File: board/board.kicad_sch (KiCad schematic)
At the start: 19 parts, among them J1 UART, J2 008_USB, J3 DebugEdge_02x05, J4 SPI_2x3, J5 ADC_2x3, J6 021_single_IO_UNIO, J7 SPI_2x3, J8 I2C_2x2, J9 UART_2x2

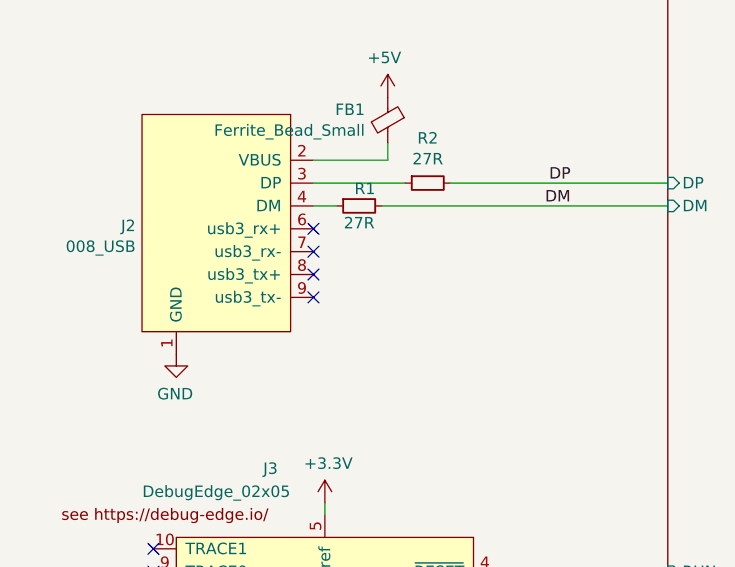
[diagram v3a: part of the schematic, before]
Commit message: upgraded to new kicad and switched to standard flash
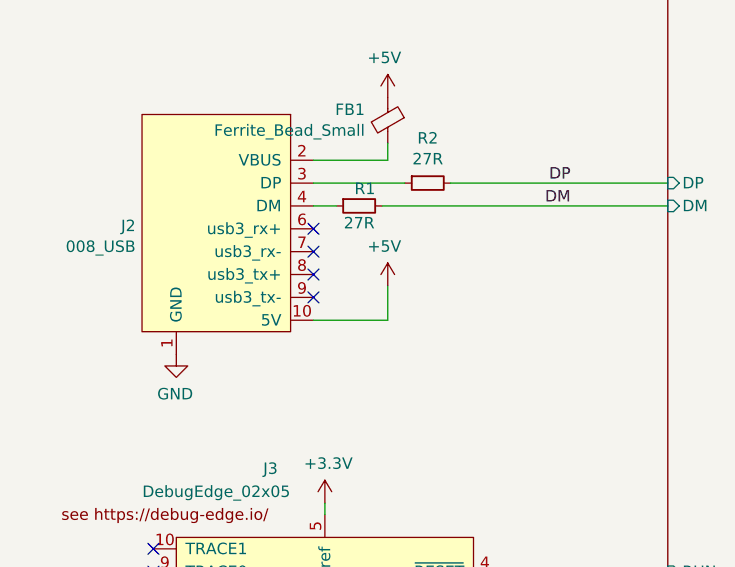
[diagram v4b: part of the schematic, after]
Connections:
- net +5V: now also J2.10 (5V)
- net +3V3 renamed +3.3V

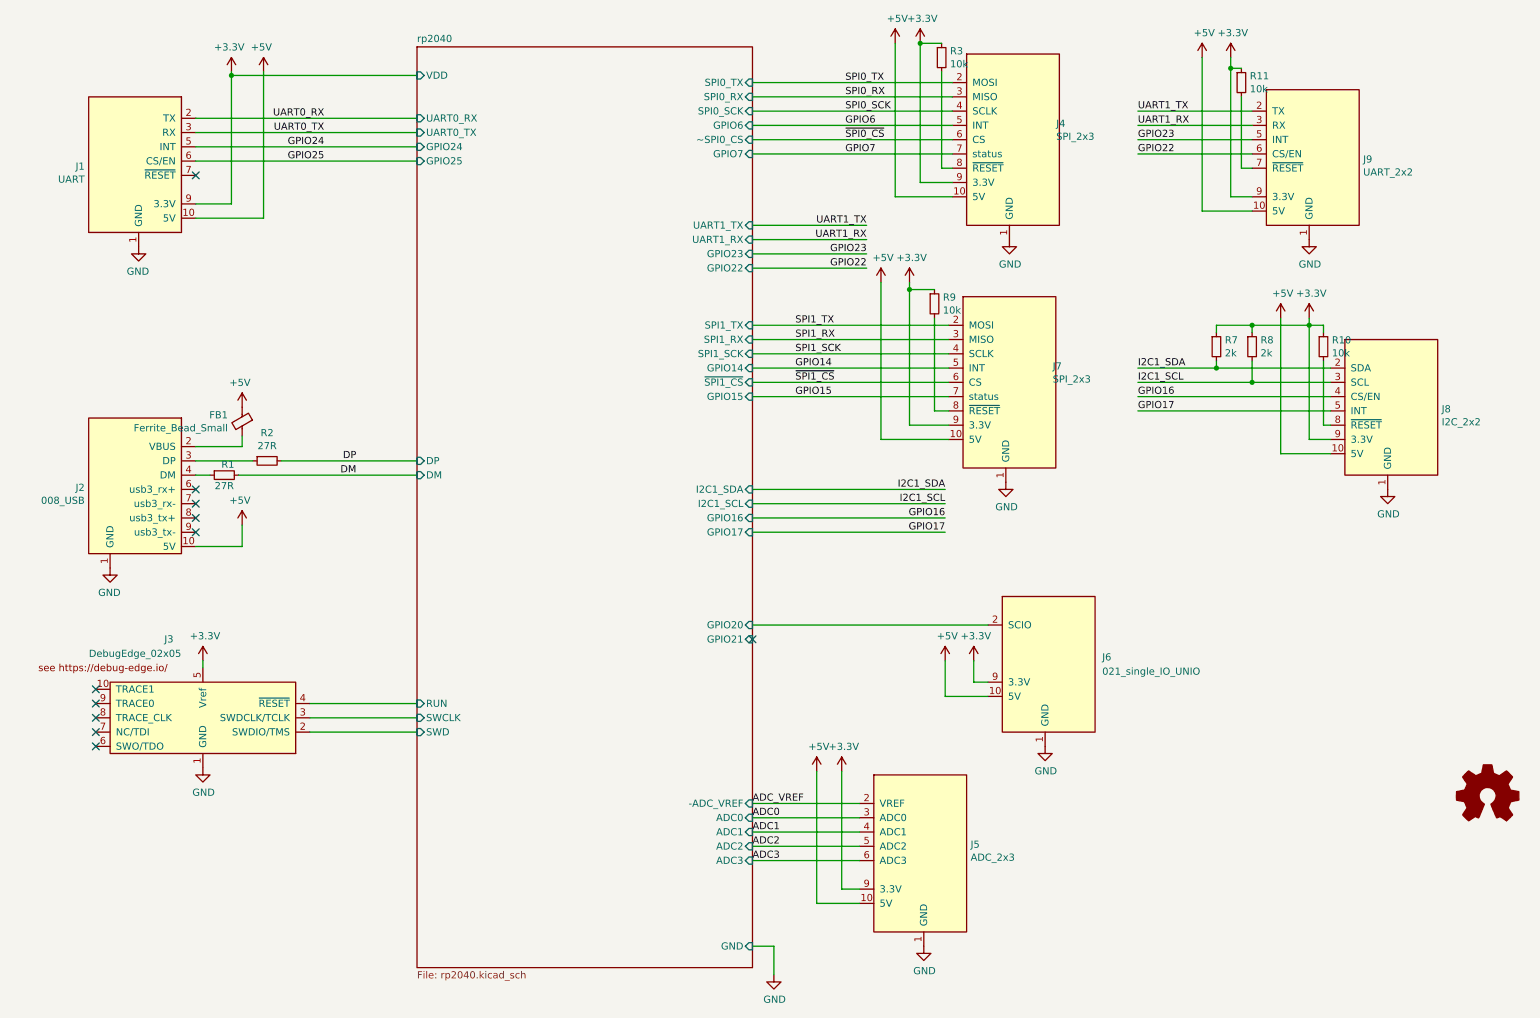
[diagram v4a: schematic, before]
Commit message: updated I2C to fixed pinning
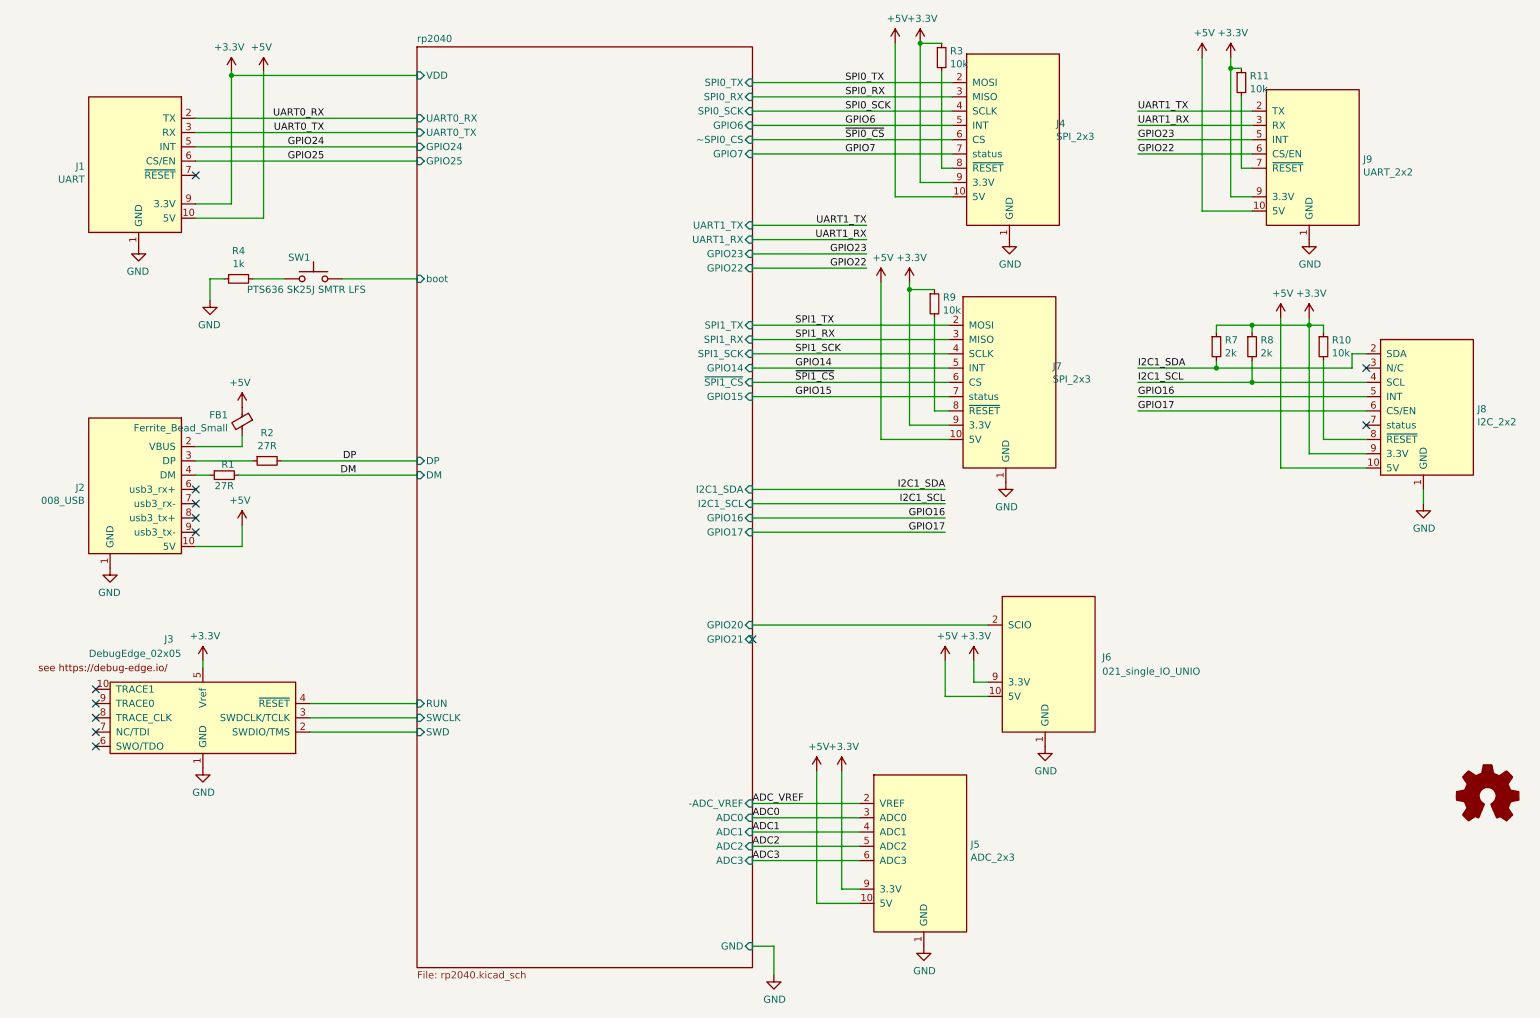
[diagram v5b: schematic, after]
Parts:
- added R4: 1k, Resistor_SMD:R_0603_1608Metric, symbol Device:R_Small
- added SW1: PTS636 SK25J SMTR LFS, Resistor_SMD:R_2512_6332Metric, symbol Switch:SW_Push
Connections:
- net GND: now also R4.1
- net GPIO16: now also J8.5 (INT); no longer J8.4 (CS/EN)
- net GPIO17: now also J8.6 (CS/EN); no longer J8.5 (INT)
- net I2C1_SCL: now also J8.4 (SCL); no longer J8.3 (SCL)
- new net: R4.2, SW1.1
- new net rp2040/boot: SW1.2
- no-connect marks 11 -> 13
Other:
- sheet rp2040 ports: added boot; removed none
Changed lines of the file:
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@@
   (no_connect (at 43.18 104.14))
   (no_connect (at 43.18 43.18))
+  (no_connect (at 251.46 77.47))
   (no_connect (at 142.24 125.73))
   (no_connect (at 25.4 142.24))
   (no_connect (at 43.18 99.06))
   (no_connect (at 43.18 106.68))
+  (no_connect (at 251.46 87.63))
   (no_connect (at 25.4 139.7))
   (no_connect (at 43.18 101.6))
@@
     (stroke (width 0) (type default))
   )
+  (wire (pts (xy 261.62 101.6) (xy 261.62 99.06))
+    (stroke (width 0) (type default))
+  )
   (wire (pts (xy 51.435 109.22) (xy 51.435 105.41))
     (stroke (width 0) (type default))
@@
     (stroke (width 0) (type default))
   )
+  (wire (pts (xy 45.72 61.595) (xy 48.26 61.595))
+    (stroke (width 0) (type default))
+  )
   (wire (pts (xy 142.24 123.19) (xy 184.15 123.19))
     (stroke (width 0) (type default))
@@
     (stroke (width 0) (type default))
   )
+  (wire (pts (xy 69.215 61.595) (xy 82.55 61.595))
+    (stroke (width 0) (type default))
+  )
   (wire (pts (xy 146.05 180.34) (xy 142.24 180.34))
     (stroke (width 0) (type default))
   )
-  (wire (pts (xy 241.3 90.17) (xy 245.11 90.17))
+  (wire (pts (xy 241.3 92.71) (xy 251.46 92.71))
     (stroke (width 0) (type default))
   )
@@
     (stroke (width 0) (type default))
   )
-  (wire (pts (xy 243.84 76.2) (xy 243.84 87.63))
-    (stroke (width 0) (type default))
-  )
-  (wire (pts (xy 236.22 92.71) (xy 245.11 92.71))
-    (stroke (width 0) (type default))
-  )
-  (wire (pts (xy 210.82 82.55) (xy 245.11 82.55))
+  (wire (pts (xy 53.34 61.595) (xy 59.055 61.595))
+    (stroke (width 0) (type default))
+  )
+  (wire (pts (xy 243.84 76.2) (xy 243.84 90.17))
+    (stroke (width 0) (type default))
+  )
+  (wire (pts (xy 236.22 95.25) (xy 251.46 95.25))
+    (stroke (width 0) (type default))
+  )
+  (wire (pts (xy 210.82 82.55) (xy 251.46 82.55))
     (stroke (width 0) (type default))
   )
@@
     (stroke (width 0) (type default))
   )
+  (wire (pts (xy 248.92 77.47) (xy 248.92 74.93))
+    (stroke (width 0) (type default))
+  )
   (wire (pts (xy 227.33 22.225) (xy 227.33 24.13))
     (stroke (width 0) (type default))
@@
     (stroke (width 0) (type default))
   )
+  (wire (pts (xy 248.92 74.93) (xy 251.46 74.93))
+    (stroke (width 0) (type default))
+  )
   (wire (pts (xy 50.8 96.52) (xy 82.55 96.52))
     (stroke (width 0) (type default))
@@
     (stroke (width 0) (type default))
   )
-  (wire (pts (xy 236.22 68.58) (xy 236.22 92.71))
+  (wire (pts (xy 236.22 68.58) (xy 236.22 95.25))
     (stroke (width 0) (type default))
   )
@@
     (stroke (width 0) (type default))
   )
-  (wire (pts (xy 243.84 87.63) (xy 245.11 87.63))
+  (wire (pts (xy 243.84 90.17) (xy 251.46 90.17))
     (stroke (width 0) (type default))
   )
@@
     (stroke (width 0) (type default))
   )
-  (wire (pts (xy 224.79 77.47) (xy 245.11 77.47))
+  (wire (pts (xy 224.79 77.47) (xy 248.92 77.47))
     (stroke (width 0) (type default))
   )
@@
     (stroke (width 0) (type default))
   )
+  (wire (pts (xy 45.72 65.405) (xy 45.72 61.595))
+    (stroke (width 0) (type default))
+  )
   (wire (pts (xy 172.085 19.685) (xy 172.085 44.45))
     (stroke (width 0) (type default))
@@
     (stroke (width 0) (type default))
   )
-  (wire (pts (xy 231.14 80.01) (xy 245.11 80.01))
+  (wire (pts (xy 231.14 80.01) (xy 251.46 80.01))
     (stroke (width 0) (type default))
   )
@@
     (stroke (width 0) (type default))
   )
-  (wire (pts (xy 241.3 69.85) (xy 241.3 90.17))
+  (wire (pts (xy 241.3 69.85) (xy 241.3 92.71))
     (stroke (width 0) (type default))
   )
@@
     (stroke (width 0) (type default))
   )
-  (wire (pts (xy 210.82 85.09) (xy 245.11 85.09))
+  (wire (pts (xy 210.82 85.09) (xy 251.46 85.09))
     (stroke (width 0) (type default))
   )
@@
     )
   )
+  (symbol (lib_id "Device:R_Small") (at 50.8 61.595 90) (mirror x) (unit 1)
+    (in_bom yes) (on_board yes) (dnp no)
+    (property "Reference" "R4" (at 50.8 56.6166 90)
+      (effects (font (size 1.27 1.27)))
+    )
+    (property "Value" "1k" (at 50.8 58.928 90)
+      (effects (font (size 1.27 1.27)))
+    )
+    (property "Footprint" "Resistor_SMD:R_0603_1608Metric" (at 50.8 61.595 0)
+      (effects (font (size 1.27 1.27)) hide)
+    )
+    (property "Datasheet" "~" (at 50.8 61.595 0)
+      (effects (font (size 1.27 1.27)) hide)
+    )
+    (pin "1")
+    (pin "2")
+    (instances
+      (project "board"
+        (path "/57732dd3-1162-4c3f-88bd-31bf473d124d"
+          (reference "R4") (unit 1)
+        )
+      )
+    )
+  )
   (symbol (lib_id "put_on_edge:010_UART") (at 31.75 41.91 0) (mirror y) (unit 1)
     (in_bom yes) (on_board yes) (dnp no)
@@
         (path "/57732dd3-1162-4c3f-88bd-31bf473d124d"
           (reference "#PWR0109") (unit 1)
+        )
+      )
+    )
+  )
+  (symbol (lib_id "Switch:SW_Push") (at 64.135 61.595 0) (unit 1)
+    (in_bom yes) (on_board yes) (dnp no)
+    (property "Reference" "SW1" (at 61.595 57.785 0)
+      (effects (font (size 1.27 1.27)))
+    )
+    (property "Value" "PTS636 SK25J SMTR LFS" (at 62.865 63.5 0)
+      (effects (font (size 1.27 1.27)))
+    )
+    (property "Footprint" "Resistor_SMD:R_2512_6332Metric" (at 64.135 56.515 0)
+      (effects (font (size 1.27 1.27)) hide)
+    )
+    (property "Datasheet" "~" (at 64.135 56.515 0)
+      (effects (font (size 1.27 1.27)) hide)
+    )
+    (property "MPN" "PTS636 SK25J SMTR LFS" (at 64.135 61.595 0)
+      (effects (font (size 1.27 1.27)) hide)
+    )
+    (pin "1")
+    (pin "2")
+    (instances
+      (project "board"
+        (path "/57732dd3-1162-4c3f-88bd-31bf473d124d"
+          (reference "SW1") (unit 1)
         )
       )
@@
     )
   )
-  (symbol (lib_id "put_on_edge:001_I2C") (at 256.54 85.09 0) (unit 1)
-    (in_bom yes) (on_board yes) (dnp no)
-    (property "Reference" "J8" (at 264.8712 84.7598 0)
-      (effects (font (size 1.27 1.27)) (justify left))
-    )
-    (property "Value" "I2C_2x2" (at 264.8712 87.0712 0)
-      (effects (font (size 1.27 1.27)) (justify left))
-    )
-    (property "Footprint" "on_edge:on_edge_2x05_host" (at 264.16 68.58 0)
-      (effects (font (size 1.27 1.27)) hide)
-    )
-    (property "Datasheet" "" (at 264.16 68.58 0)
+  (symbol (lib_id "put_on_edge:001_I2C") (at 262.89 85.09 0) (unit 1)
+    (in_bom yes) (on_board yes) (dnp no)
+    (property "Reference" "J8" (at 271.2212 84.7598 0)
+      (effects (font (size 1.27 1.27)) (justify left))
+    )
+    (property "Value" "I2C_2x2" (at 271.2212 87.0712 0)
+      (effects (font (size 1.27 1.27)) (justify left))
+    )
+    (property "Footprint" "on_edge:on_edge_2x05_host" (at 270.51 68.58 0)
+      (effects (font (size 1.27 1.27)) hide)
+    )
+    (property "Datasheet" "" (at 270.51 68.58 0)
       (effects (font (size 1.27 1.27)) hide)
     )
@@
     (pin "8")
     (pin "9")
+    (pin "6")
+    (pin "7")
     (instances
       (project "board"
@@
     )
   )
-  (symbol (lib_id "power:GND") (at 255.27 99.06 0) (unit 1)
-    (in_bom yes) (on_board yes) (dnp no)
-    (property "Reference" "#PWR0104" (at 255.27 105.41 0)
-      (effects (font (size 1.27 1.27)) hide)
-    )
-    (property "Value" "GND" (at 255.397 103.4542 0)
-      (effects (font (size 1.27 1.27)))
-    )
-    (property "Footprint" "" (at 255.27 99.06 0)
-      (effects (font (size 1.27 1.27)) hide)
-    )
-    (property "Datasheet" "" (at 255.27 99.06 0)
+  (symbol (lib_id "power:GND") (at 261.62 101.6 0) (unit 1)
+    (in_bom yes) (on_board yes) (dnp no)
+    (property "Reference" "#PWR0104" (at 261.62 107.95 0)
+      (effects (font (size 1.27 1.27)) hide)
+    )
+    (property "Value" "GND" (at 261.747 105.9942 0)
+      (effects (font (size 1.27 1.27)))
+    )
+    (property "Footprint" "" (at 261.62 101.6 0)
+      (effects (font (size 1.27 1.27)) hide)
+    )
+    (property "Datasheet" "" (at 261.62 101.6 0)
       (effects (font (size 1.27 1.27)) hide)
     )
@@
     )
   )
+  (symbol (lib_id "power:GND") (at 45.72 65.405 0) (mirror y) (unit 1)
+    (in_bom yes) (on_board yes) (dnp no)
+    (property "Reference" "#PWR02" (at 45.72 71.755 0)
+      (effects (font (size 1.27 1.27)) hide)
+    )
+    (property "Value" "GND" (at 45.593 69.7992 0)
+      (effects (font (size 1.27 1.27)))
+    )
+    (property "Footprint" "" (at 45.72 65.405 0)
+      (effects (font (size 1.27 1.27)) hide)
+    )
+    (property "Datasheet" "" (at 45.72 65.405 0)
+      (effects (font (size 1.27 1.27)) hide)
+    )
+    (pin "1")
+    (instances
+      (project "board"
+        (path "/57732dd3-1162-4c3f-88bd-31bf473d124d"
+          (reference "#PWR02") (unit 1)
+        )
+      )
+    )
+  )
   (symbol (lib_id "power:GND") (at 187.96 54.61 0) (unit 1)
     (in_bom yes) (on_board yes) (dnp no)
@@
       (effects (font (size 1.27 1.27)) (justify left))
     )
+    (pin "boot" input (at 82.55 61.595 180)
+      (effects (font (size 1.27 1.27)) (justify left))
+    )
